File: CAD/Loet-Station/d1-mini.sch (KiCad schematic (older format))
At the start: 1 part, among them U301 WeMos_D1_mini

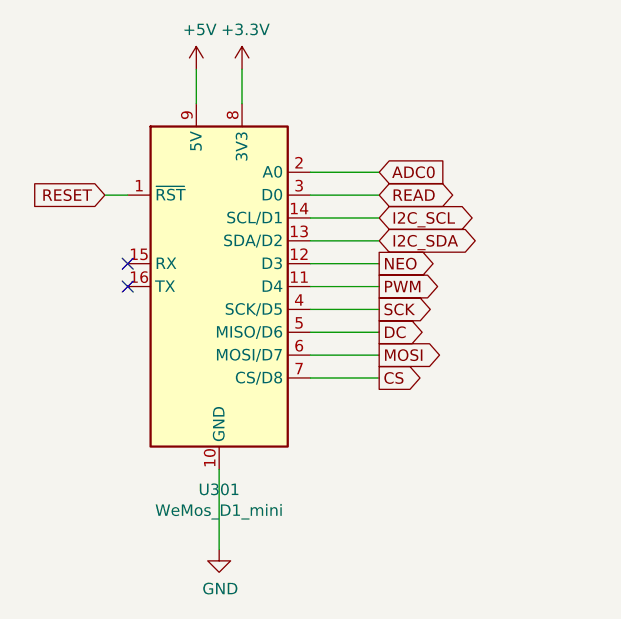
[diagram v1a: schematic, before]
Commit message: changed d1 mini pins, optional i2c oled
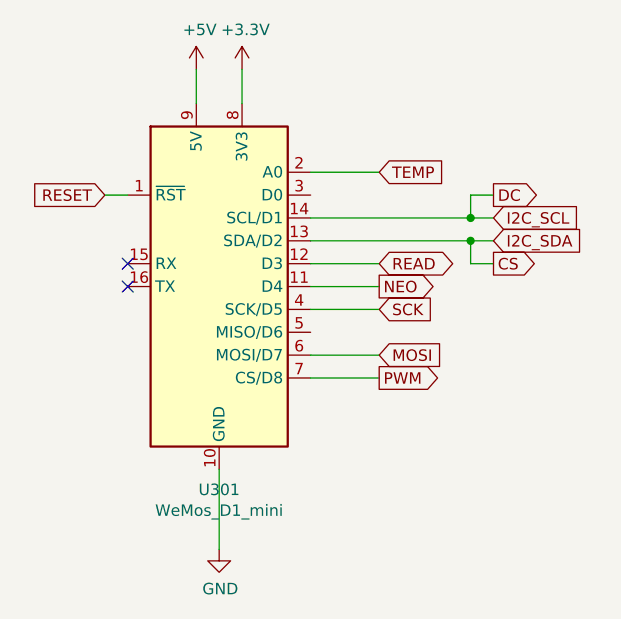
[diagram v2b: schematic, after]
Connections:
- net I2C_SCL is gone; now on net DC: U301.14 (SCL/D1)
- net I2C_SDA is gone; now on net CS: U301.13 (SDA/D2)
- net CS: no longer U301.7 (CS/D8)
- net DC: no longer U301.5 (MISO/D6)
- net NEO: now also U301.11 (D4); no longer U301.12 (D3)
- net PWM: now also U301.7 (CS/D8); no longer U301.11 (D4)
- net READ: now also U301.12 (D3); no longer U301.3 (D0)
- net ADC0 renamed TEMP
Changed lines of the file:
@@
 $Descr A4 11693 8268
 encoding utf-8
-Sheet 3 7
+Sheet 3 6
 Title ""
 Date ""
@@
 Comment4 ""
 $EndDescr
+Text GLabel 6150 3250 2    50   Output ~ 0
+CS
+Text GLabel 5650 3350 2    50   Output ~ 0
+NEO
 Text GLabel 5650 3750 2    50   Output ~ 0
-CS
-Text GLabel 5650 3250 2    50   Output ~ 0
-NEO
-Text GLabel 5650 3350 2    50   Output ~ 0
 PWM
 $Comp
@@
 Wire Wire Line
 	4950 4150 4950 4500
-Text GLabel 5650 3650 2    50   Output ~ 0
-MOSI
-Text GLabel 5650 3450 2    50   Output ~ 0
-SCK
-Text GLabel 5650 3550 2    50   Output ~ 0
+Text GLabel 6150 2950 2    50   Output ~ 0
 DC
-Text GLabel 5650 2950 2    50   BiDi ~ 0
+Text GLabel 5650 3250 2    50   BiDi ~ 0
 READ
 Text GLabel 4450 2950 0    50   Input ~ 0
@@
 Wire Wire Line
 	4450 2950 4550 2950
-Wire Wire Line
-	5350 3450 5650 3450
-Wire Wire Line
-	5350 2950 5650 2950
-Wire Wire Line
-	5350 3250 5650 3250
-Wire Wire Line
-	5350 3350 5650 3350
-Text GLabel 5650 3050 2    50   BiDi ~ 0
-I2C_SCL
-Text GLabel 5650 3150 2    50   BiDi ~ 0
-I2C_SDA
-Wire Wire Line
-	5350 3050 5650 3050
-Wire Wire Line
-	5350 3150 5650 3150
-Text GLabel 5650 2850 2    50   Input ~ 0
-ADC0
-Wire Wire Line
-	5350 2850 5650 2850
 NoConn ~ 4550 3250
 NoConn ~ 4550 3350
-Wire Wire Line
-	5350 3750 5650 3750
-Wire Wire Line
-	5350 3650 5650 3650
-Wire Wire Line
-	5350 3550 5650 3550
 $Comp
 L MCU_Module:WeMos_D1_mini U?
@@
 Wire Wire Line
 	5050 2400 5050 2550
+Text GLabel 5650 3650 2    50   Input ~ 0
+MOSI
+Text GLabel 5650 3450 2    50   Input ~ 0
+SCK
+Wire Wire Line
+	5350 3350 5650 3350
+Wire Wire Line
+	5350 3750 5650 3750
+Text GLabel 5650 2850 2    50   Input ~ 0
+TEMP
+Wire Wire Line
+	5350 2850 5650 2850
+Wire Wire Line
+	5350 3250 5650 3250
+Wire Wire Line
+	5350 3450 5650 3450
+Wire Wire Line
+	5350 3650 5650 3650
+Text GLabel 6150 3050 2    50   Input ~ 0
+I2C_SCL
+Text GLabel 6150 3150 2    50   Input ~ 0
+I2C_SDA
+Wire Wire Line
+	5350 3050 6050 3050
+Wire Wire Line
+	5350 3150 6050 3150
+Wire Wire Line
+	6150 2950 6050 2950
+Wire Wire Line
+	6050 2950 6050 3050
+Connection ~ 6050 3050
+Wire Wire Line
+	6050 3050 6150 3050
+Wire Wire Line
+	6150 3250 6050 3250
+Wire Wire Line
+	6050 3250 6050 3150
+Connection ~ 6050 3150
+Wire Wire Line
+	6050 3150 6150 3150
 $EndSCHEMATC
